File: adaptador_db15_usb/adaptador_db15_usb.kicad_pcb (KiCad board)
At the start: 2 copper layers, 100 x 92.6 mm, 32 parts, among them J1 Conn_01x08_Female, J1 Conn_01x34, J2 A-USB3_A-LP-SMT1, J2 Conn_01x04_Male, J3 A-USB3_A-LP-SMT1, U1 M95XXX

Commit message: Changed PCB
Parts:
- removed the J1 at (119.3, 122.7)
- removed the J1 at (119.3, 105.9)
- removed the J1 at (138.9, 105.9)
- removed the J1 at (138.9, 122.8)
- removed the J2 at (116.3, 130.6)
- removed the J2 at (116.2, 113.7)
- removed the J2 at (135.8, 113.7)
- removed the J2 at (135.8, 130.6)
- removed R1 (x4), R2 (x4): R, Resistor_SMD:R_0805_2012Metric_Pad1.20x1.40mm_HandSolder
- removed U1 (x4): M95XXX, Package_SO:SOIC-8_3.9x4.9mm_P1.27mm
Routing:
- net /5v: track 77.8 -> 0.00 mm
- net /Mosi: track 66.3 -> 0.00 mm
- net /clk: track 65.7 -> 0.00 mm
- net /miso: track 34.4 -> 0.00 mm
- net /cs: track 25.2 -> 0.00 mm
- net Net-(R1-Pad1): track 12.9 -> 0.00 mm
- net Net-(R2-Pad1): track 12.2 -> 0.00 mm
- net /0v1: track 81.0 -> 84.4 mm
- net /0v2: track 144.0 -> 146.9 mm
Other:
- outline, holes or cut-outs redrawn
- board text removed: "IOT Group-Memory adapter"
- board text removed: "~S~ Q C D"

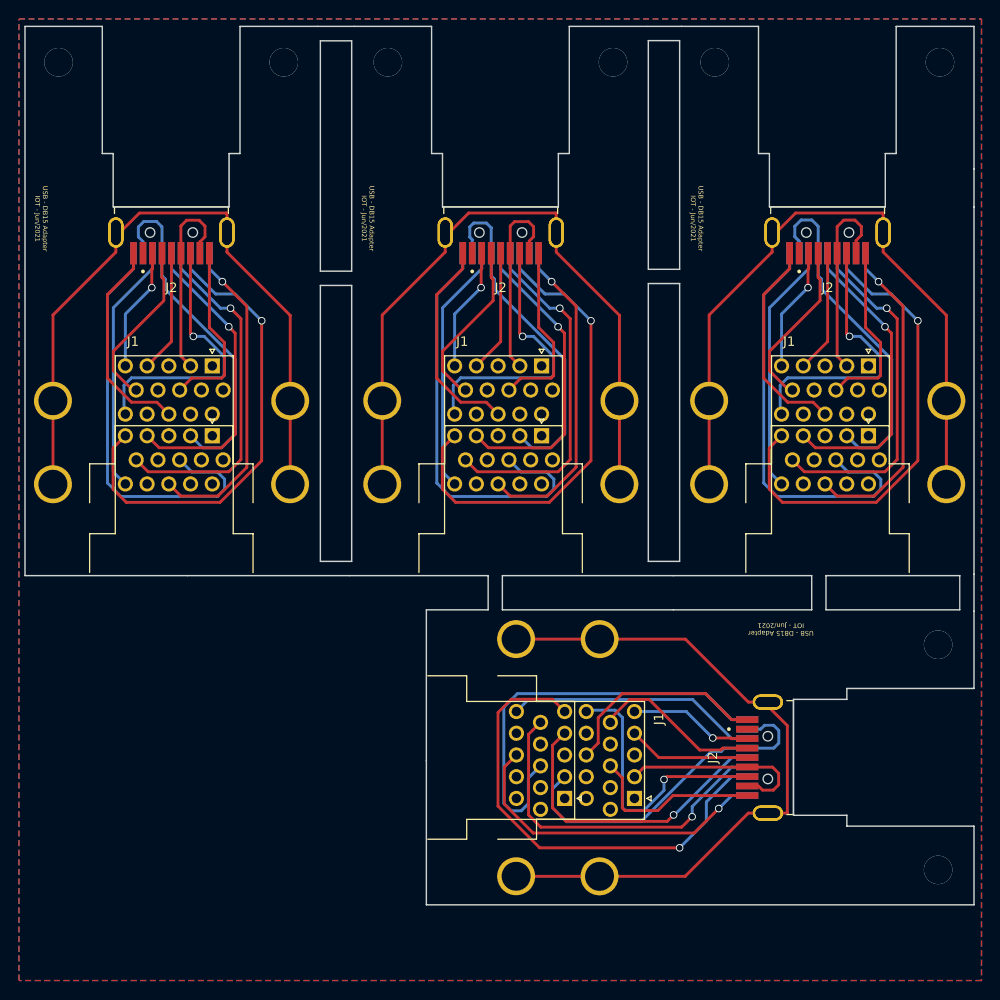
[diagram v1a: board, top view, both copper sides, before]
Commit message: Fixed adapter pins connections
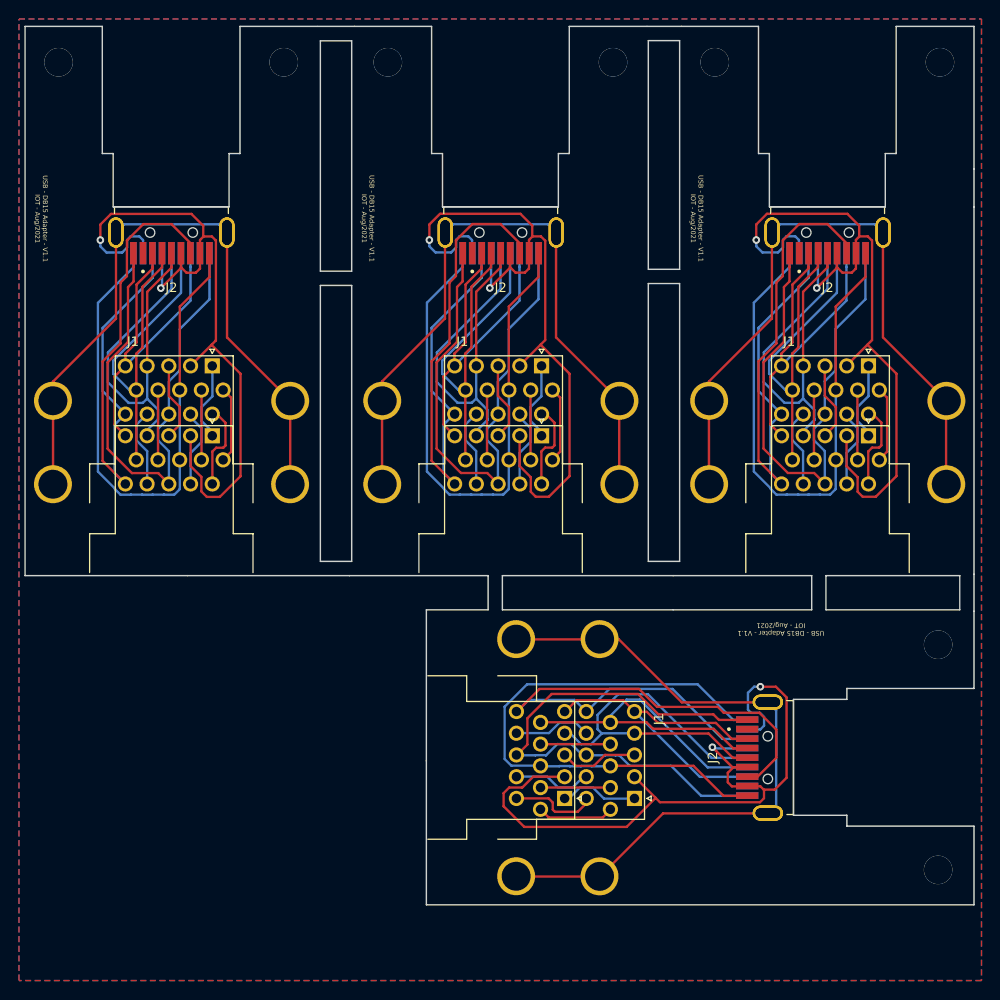
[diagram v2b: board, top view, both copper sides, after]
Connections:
- J1 pad 1: Net-(J1-Pad1) -> /[1] (x4)
- J1 pad 10: /sensor0v1 -> /[10] (x4)
- J1 pad 11: Net-(J1-Pad11) -> /[11] (x4)
- J1 pad 12: /sensorup1 -> /[12] (x4)
- J1 pad 14: Net-(J1-Pad14) -> /[14] (x4)
- J1 pad 17: /0v2 -> /0v1 (x4)
- J1 pad 28: /-data2 -> /-data1 (x4)
- J1 pad 3: Net-(J1-Pad3) -> /[3] (x4)
- J1 pad 30: /-clock2 -> /-clock1 (x4)
- J1 pad 4: /up1 -> /[4] (x4)
- J1 pad 5: /data1 -> /[5] (x4)
- J1 pad 6: Net-(J1-Pad6) -> /[6] (x4)
- J1 pad 7: Net-(J1-Pad7) -> /[7] (x4)
- J1 pad 8: /clock1 -> /[8] (x4)
- J1 pad 9: Net-(J1-Pad9) -> /[9] (x4)
- J2 pad 2: /sensor0v1 -> /[10] (x4)
- J2 pad 5: /clock1 -> /[8] (x4)
- J2 pad 7: /up1 -> /[4] (x4)
- J2 pad 8: /data1 -> /[5] (x4)
- J3 pad 3: /0v2 -> /0v1 (x4)
- J3 pad 4: /0v2 -> /0v1 (x4)
- J3 pad 6: /-clock2 -> /-clock1 (x4)
- J3 pad 9: /-data2 -> /-data1 (x4)
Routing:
- net /0v1: track 84.4 -> 318.2 mm, vias 0 -> 8
- net /0v2: track 146.9 -> 0.00 mm
- net /-clock1: track 116.4 -> 261.8 mm, vias 4 -> 0
- net /-data1: track 89.4 -> 227.2 mm
- net /-data2: track 136.8 -> 0.00 mm, vias 4 -> 0
- net /-clock2: track 106.2 -> 0.00 mm
- net /clock1: track 75.5 -> 0.00 mm
- net /sensor0v1: track 71.7 -> 0.00 mm
- net /[8]: track 180.9 -> 243.1 mm
- net /[5]: track 201.5 -> 144.4 mm, vias 4 -> 0
- net /data1: track 52.3 -> 0.00 mm, vias 4 -> 0
- net /up1: track 51.8 -> 0.00 mm
- net /[4]: track 129.1 -> 171.6 mm, vias 4 -> 0
- net /[11]: track 0.00 -> 36.9 mm
- net /[3]: track 0.00 -> 33.3 mm
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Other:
- board text added: "USB - DB15 Adapter - V1.1 IOT - Aug/2021"
- board text removed: "USB - DB15 Adapter IOT - Jun/2021"

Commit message: Fixed adapter pins connections
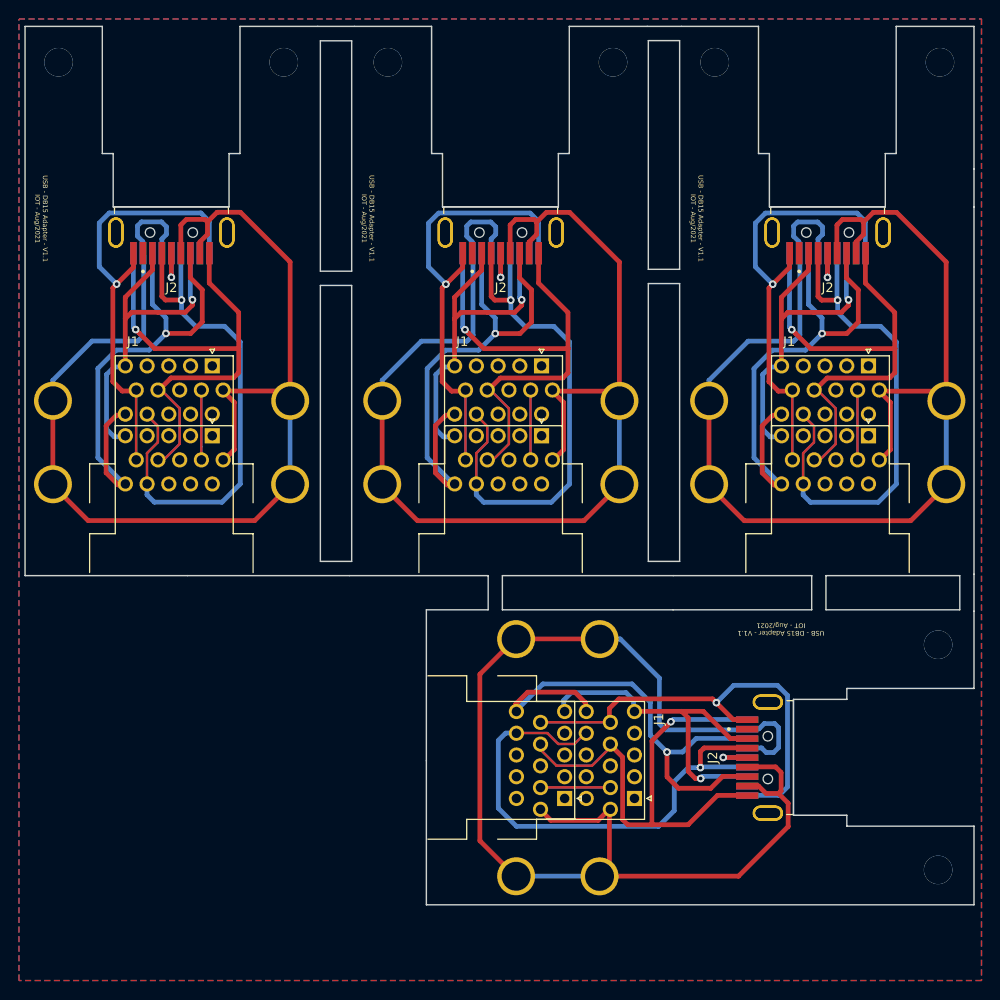
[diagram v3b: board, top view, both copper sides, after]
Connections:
- net /[5] renamed /data1
- net /[7] renamed /+9v
- J1 pad 1: /[1] -> Net-(J1-Pad1) (x4)
- J1 pad 10: /[10] -> /-data1 (x4)
- J1 pad 11: /[11] -> Net-(J1-Pad11) (x4)
- J1 pad 12: /[12] -> Net-(J1-Pad12) (x4)
- J1 pad 13: /-data1 -> Net-(J1-Pad13) (x4)
- J1 pad 14: /[14] -> /sensorup1 (x4)
- J1 pad 16: /[1] -> Net-(J1-Pad16) (x4)
- J1 pad 17: /0v1 -> Net-(J1-Pad17) (x4)
- J1 pad 18: /[3] -> Net-(J1-Pad18) (x4)
- J1 pad 19: /[4] -> Net-(J1-Pad19) (x4)
- J1 pad 2: /0v1 -> Net-(J1-Pad2) (x4)
- J1 pad 21: /[6] -> /0v1 (x4)
- J1 pad 23: /[8] -> Net-(J1-Pad23) (x4)
- J1 pad 24: /[9] -> /clock1 (x4)
- J1 pad 25: /[10] -> /-data1 (x4)
- J1 pad 26: /[11] -> Net-(J1-Pad26) (x4)
- J1 pad 27: /[12] -> Net-(J1-Pad27) (x4)
- J1 pad 28: /-data1 -> Net-(J1-Pad28) (x4)
- J1 pad 29: /[14] -> /sensorup1 (x4)
- J1 pad 3: /[3] -> Net-(J1-Pad3) (x4)
- J1 pad 31: Net-(J1-Pad31) -> /0v1 (x4)
- J1 pad 32: Net-(J1-Pad31) -> /0v1 (x4)
- J1 pad 33: Net-(J1-Pad31) -> /0v1 (x4)
- J1 pad 34: Net-(J1-Pad31) -> /0v1 (x4)
- J1 pad 4: /[4] -> Net-(J1-Pad4) (x4)
- J1 pad 6: /[6] -> /0v1 (x4)
- J1 pad 8: /[8] -> Net-(J1-Pad8) (x4)
- J1 pad 9: /[9] -> /clock1 (x4)
- J2 pad 2: /[10] -> /sensorup1 (x4)
- J2 pad 5: /[8] -> /clock1 (x4)
- J2 pad 7: /[4] -> /up1 (x4)
- J2 pad S1: Net-(J1-Pad31) -> Net-(J2-PadS1) (x4)
- J2 pad S2: Net-(J1-Pad31) -> Net-(J2-PadS2) (x4)
- J3 pad 2: /[10] -> /sensorup1 (x4)
- J3 pad 5: /[8] -> /clock1 (x4)
- J3 pad 7: /[4] -> /up1 (x4)
- J3 pad S1: Net-(J1-Pad31) -> Net-(J3-PadS1) (x4)
- J3 pad S2: Net-(J1-Pad31) -> Net-(J3-PadS2) (x4)
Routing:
- net Net-(J1-Pad31): track 283.9 -> 0.00 mm
- net /sensorup1: track 0.00 -> 255.6 mm, vias 0 -> 4
- net /clock1: track 0.00 -> 248.9 mm, vias 0 -> 4
- net /[8]: track 243.1 -> 0.00 mm
- net /0v1: track 318.2 -> 519.0 mm, vias 8 -> 0
- net /[4]: track 171.6 -> 0.00 mm
- net /[10]: track 167.0 -> 0.00 mm
- net /-clock1: track 261.8 -> 212.4 mm, vias 0 -> 4
- net /[11]: track 36.9 -> 0.00 mm
- net /[3]: track 33.3 -> 0.00 mm
- net /[14]: track 33.3 -> 0.00 mm
- net /[1]: track 33.2 -> 0.00 mm
- net /[12]: track 33.2 -> 0.00 mm
- net /[6]: track 32.2 -> 0.00 mm
- net /+9v: track 29.5 -> 59.1 mm
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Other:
- net class Default: trace_width 0.25 -> 0.35
